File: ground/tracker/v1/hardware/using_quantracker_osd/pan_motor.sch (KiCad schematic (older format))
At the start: 20 parts, among them K4 CONN_3, P2 CONN_4, P3 CONN_5, U4 SI8620, U5 74AHC1G04

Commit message: add i2c and gps connectors
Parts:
- C18: renamed from C21; value C -> 0.1uF; footprint (none) -> SMD_0603:SMD_0603
- renumbered C22 to C19, C23 to C20, C24 to C21, C25 to C22, C26 to C23, C27 to C24, C28 to C25, C29 to C26
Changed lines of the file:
@@
 +5V
 $Comp
-L C C21
+L C C18
 U 1 1 587FB33F
 P 2325 7125
-F 0 "C21" H 2350 7225 50  0000 L CNN
-F 1 "C" H 2350 7025 50  0000 L CNN
-F 2 "" H 2363 6975 50  0000 C CNN
+F 0 "C18" H 2350 7225 50  0000 L CNN
+F 1 "0.1uF" H 2350 7025 50  0000 L CNN
+F 2 "SMD_0603:SMD_0603" H 2363 6975 50  0001 C CNN
 F 3 "" H 2325 7125 50  0000 C CNN
 	1    2325 7125
@@
 $EndComp
 $Comp
-L C C22
+L C C19
 U 1 1 587FB43C
 P 4525 3800
-F 0 "C22" H 4550 3900 50  0000 L CNN
+F 0 "C19" H 4550 3900 50  0000 L CNN
 F 1 "C" H 4550 3700 50  0000 L CNN
 F 2 "" H 4563 3650 50  0000 C CNN
@@
 $EndComp
 $Comp
-L C C23
+L C C20
 U 1 1 587FB7FF
 P 4800 3800
-F 0 "C23" H 4825 3900 50  0000 L CNN
+F 0 "C20" H 4825 3900 50  0000 L CNN
 F 1 "C" H 4825 3700 50  0000 L CNN
 F 2 "" H 4838 3650 50  0000 C CNN
@@
 $EndComp
 $Comp
-L CAP3T C25
+L CAP3T C22
 U 1 1 587FBE06
 P 6625 2125
-F 0 "C25" H 6775 1875 60  0000 C CNN
+F 0 "C22" H 6775 1875 60  0000 C CNN
 F 1 "NFM18PS105R0J3" H 6825 2375 60  0000 C CNN
 F 2 "" H 6625 2125 60  0001 C CNN
@@
 NoConn ~ 10125 5775
 $Comp
-L CAP3T C29
+L CAP3T C26
 U 1 1 587FE706
 P 9275 5075
-F 0 "C29" H 9425 4825 60  0000 C CNN
+F 0 "C26" H 9425 4825 60  0000 C CNN
 F 1 "NFM31PC276B0J3" H 9475 5325 60  0000 C CNN
 F 2 "" H 9275 5075 60  0001 C CNN
@@
 	6250 6225 5550 6225
 $Comp
-L CAP3T C24
+L CAP3T C21
 U 1 1 587FF1BF
 P 5300 6225
-F 0 "C24" H 5450 5975 60  0000 C CNN
+F 0 "C21" H 5450 5975 60  0000 C CNN
 F 1 "NFM18PS105R0J3" H 5500 6475 60  0000 C CNN
 F 2 "" H 5300 6225 60  0001 C CNN
@@
 	3750 5350 2075 5350
 $Comp
-L CP1 C27
+L CP1 C24
 U 1 1 58801015
 P 8450 5500
-F 0 "C27" H 8475 5600 50  0000 L CNN
+F 0 "C24" H 8475 5600 50  0000 L CNN
 F 1 "CP1" H 8475 5400 50  0000 L CNN
 F 2 "" H 8450 5500 50  0000 C CNN
@@
 $EndComp
 $Comp
-L CP1 C28
+L CP1 C25
 U 1 1 58801095
 P 8750 5500
-F 0 "C28" H 8775 5600 50  0000 L CNN
+F 0 "C25" H 8775 5600 50  0000 L CNN
 F 1 "CP1" H 8775 5400 50  0000 L CNN
 F 2 "" H 8750 5500 50  0000 C CNN
@@
 Pan Motor power
 $Comp
-L C C26
+L C C23
 U 1 1 5880246B
 P 7775 5525
-F 0 "C26" H 7800 5625 50  0000 L CNN
+F 0 "C23" H 7800 5625 50  0000 L CNN
 F 1 "C" H 7800 5425 50  0000 L CNN
 F 2 "" H 7813 5375 50  0000 C CNN
@@
 $EndComp
 $Comp
-L PWR_FLAG #FLG09
+L PWR_FLAG #FLG010
 U 1 1 58820405
 P 7825 4025
-F 0 "#FLG09" H 7825 4120 50  0001 C CNN
+F 0 "#FLG010" H 7825 4120 50  0001 C CNN
 F 1 "PWR_FLAG" H 7825 4205 50  0000 C CNN
 F 2 "" H 7825 4025 50  0000 C CNN
@@
 Connection ~ 7825 4225
 $Comp
-L PWR_FLAG #FLG010
+L PWR_FLAG #FLG011
 U 1 1 58820682
 P 8125 1950
-F 0 "#FLG010" H 8125 2045 50  0001 C CNN
+F 0 "#FLG011" H 8125 2045 50  0001 C CNN
 F 1 "PWR_FLAG" H 8125 2130 50  0000 C CNN
 F 2 "" H 8125 1950 50  0000 C CNN
@@
 Connection ~ 8125 2125
 $Comp
-L PWR_FLAG #FLG011
+L PWR_FLAG #FLG012
 U 1 1 58820928
 P 5025 2000
-F 0 "#FLG011" H 5025 2095 50  0001 C CNN
+F 0 "#FLG012" H 5025 2095 50  0001 C CNN
 F 1 "PWR_FLAG" H 5025 2180 50  0000 C CNN
 F 2 "" H 5025 2000 50  0000 C CNN

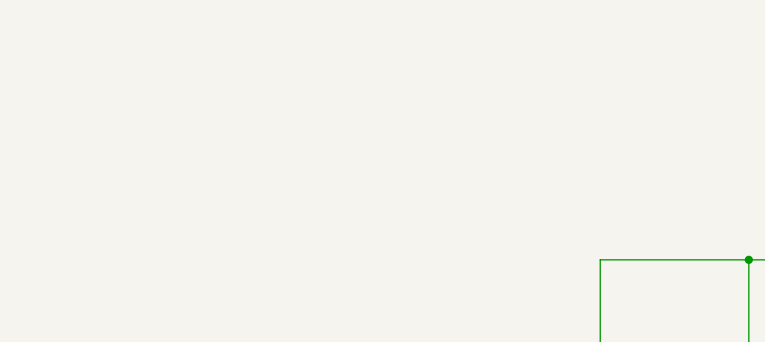
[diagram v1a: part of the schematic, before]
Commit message: add emf and currnt feedback opton
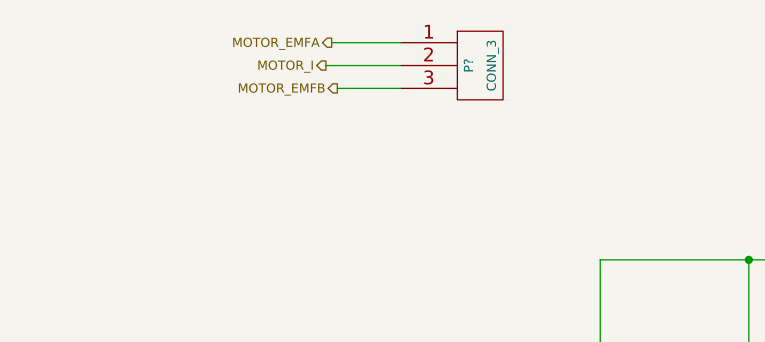
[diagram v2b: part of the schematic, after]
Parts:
- added P?: CONN_3, symbol CONN_3
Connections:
- new net MOTOR_EMFA: P?.1 (P1)
- new net MOTOR_EMFB: P?.3 (P3)
- new net MOTOR_I: P?.2 (PM)
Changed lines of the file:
@@
 	5025 2000 5025 2125
 Connection ~ 5025 2125
+$Comp
+L CONN_3 P?
+U 1 1 588A3767
+P 3350 1275
+F 0 "P?" V 3300 1275 40  0000 C CNN
+F 1 "CONN_3" V 3400 1275 40  0000 C CNN
+F 2 "" H 3350 1275 60  0001 C CNN
+F 3 "" H 3350 1275 60  0001 C CNN
+	1    3350 1275
+	1    0    0    -1
+$EndComp
+Text HLabel 2700 1175 0    40   Output ~ 0
+MOTOR_EMFA
+Text HLabel 2725 1375 0    40   Output ~ 0
+MOTOR_EMFB
+Wire Wire Line
+	3000 1175 2700 1175
+Wire Wire Line
+	3000 1375 2725 1375
+Text HLabel 2675 1275 0    40   Output ~ 0
+MOTOR_I
+Wire Wire Line
+	3000 1275 2675 1275
 $EndSCHEMATC

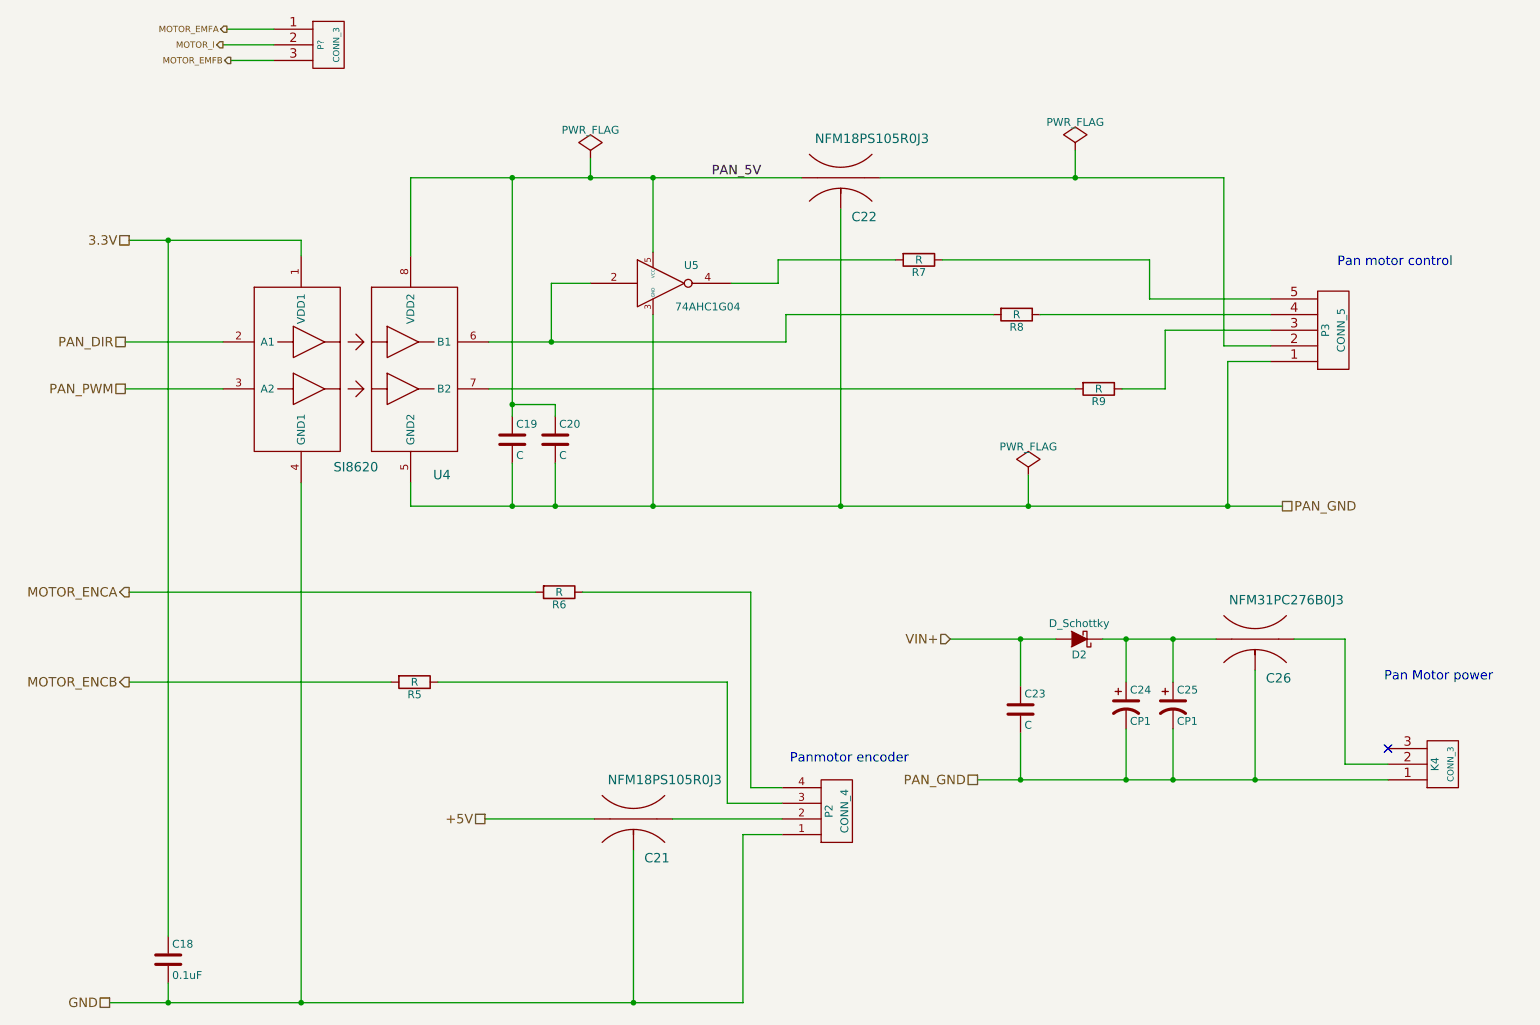
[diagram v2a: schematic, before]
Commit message: move encoder up out of pan motor schematic
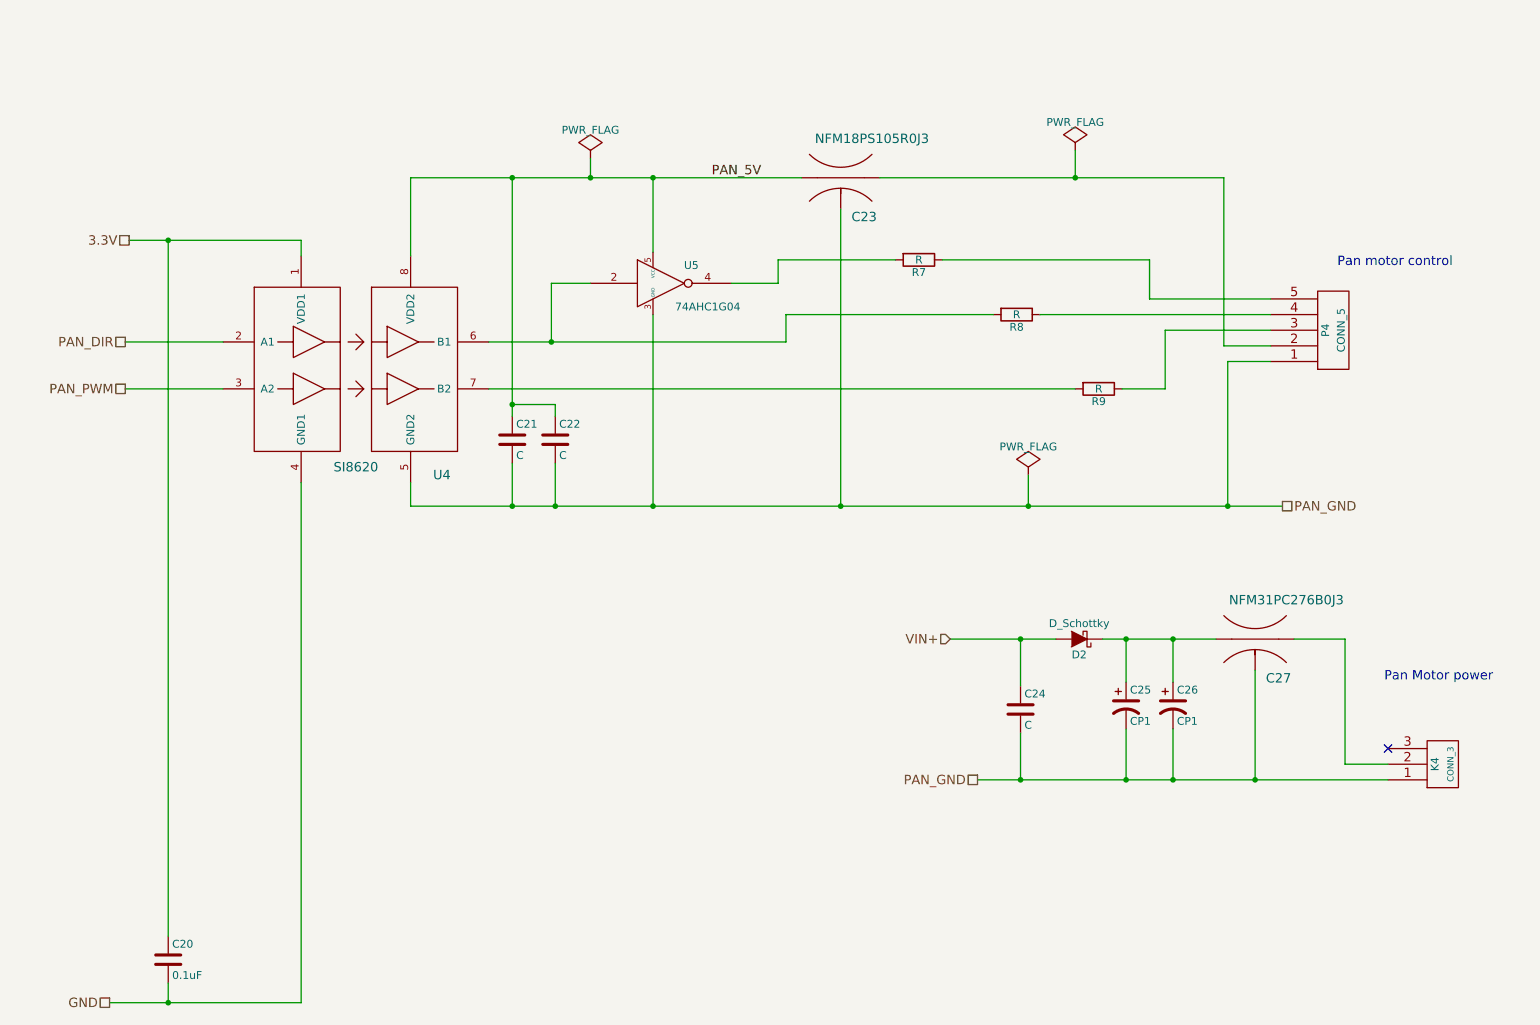
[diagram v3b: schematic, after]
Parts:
- removed C21: NFM18PS105R0J3, symbol CAP3T
- removed P2: CONN_4, symbol CONN_4
- removed P?: CONN_3, symbol CONN_3
- removed R5, R6: R, symbol R
- renumbered C18 to C20, C19 to C21, C20 to C22, C22 to C23, C23 to C24, C24 to C25, C25 to C26, C26 to C27, P3 to P4
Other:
- note removed: "Panmotor encoder"
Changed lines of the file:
@@
 $EndComp
 $Comp
-L CONN_5 P3
+L CONN_5 P4
 U 1 1 587F798A
 P 9775 3100
-F 0 "P3" V 9725 3100 50  0000 C CNN
+F 0 "P4" V 9725 3100 50  0000 C CNN
 F 1 "CONN_5" V 9825 3100 50  0000 C CNN
 F 2 "" H 9775 3100 60  0001 C CNN
@@
 	1    0    0    1
 $EndComp
-$Comp
-L CONN_4 P2
-U 1 1 587F7991
-P 6600 6175
-F 0 "P2" V 6550 6175 50  0000 C CNN
-F 1 "CONN_4" V 6650 6175 50  0000 C CNN
-F 2 "" H 6600 6175 60  0001 C CNN
-F 3 "" H 6600 6175 60  0001 C CNN
-	1    6600 6175
-	1    0    0    1
-$EndComp
 Text Notes 9800 2700 0    60   ~ 0
 Pan motor control
-Text Notes 6300 5875 0    60   ~ 0
-Panmotor encoder
 Text HLabel 2075 2525 0    60   UnSpc ~ 0
 3.3V
@@
 Text Label 5800 2125 0    60   ~ 0
 PAN_5V
-Text HLabel 2075 4775 0    60   Output ~ 0
-MOTOR_ENCA
-Text HLabel 2075 5350 0    60   Output ~ 0
-MOTOR_ENCB
-Text HLabel 4350 6225 0    60   UnSpc ~ 0
-+5V
-$Comp
-L C C18
+$Comp
+L C C20
 U 1 1 587FB33F
 P 2325 7125
-F 0 "C18" H 2350 7225 50  0000 L CNN
+F 0 "C20" H 2350 7225 50  0000 L CNN
 F 1 "0.1uF" H 2350 7025 50  0000 L CNN
 F 2 "SMD_0603:SMD_0603" H 2363 6975 50  0001 C CNN
@@
 $EndComp
 $Comp
-L C C19
+L C C21
 U 1 1 587FB43C
 P 4525 3800
-F 0 "C19" H 4550 3900 50  0000 L CNN
+F 0 "C21" H 4550 3900 50  0000 L CNN
 F 1 "C" H 4550 3700 50  0000 L CNN
 F 2 "" H 4563 3650 50  0000 C CNN
@@
 $EndComp
 $Comp
-L C C20
+L C C22
 U 1 1 587FB7FF
 P 4800 3800
-F 0 "C20" H 4825 3900 50  0000 L CNN
+F 0 "C22" H 4825 3900 50  0000 L CNN
 F 1 "C" H 4825 3700 50  0000 L CNN
 F 2 "" H 4838 3650 50  0000 C CNN
@@
 $EndComp
 $Comp
-L CAP3T C22
+L CAP3T C23
 U 1 1 587FBE06
 P 6625 2125
-F 0 "C22" H 6775 1875 60  0000 C CNN
+F 0 "C23" H 6775 1875 60  0000 C CNN
 F 1 "NFM18PS105R0J3" H 6825 2375 60  0000 C CNN
 F 2 "" H 6625 2125 60  0001 C CNN
@@
 	3875 4225 3875 4075
 Wire Wire Line
-	1950 7400 6000 7400
+	1950 7400 3175 7400
 Wire Wire Line
 	3175 7400 3175 4075
@@
 Wire Wire Line
 	6875 2125 9075 2125
-Connection ~ 3175 7400
 Wire Wire Line
 	2325 6975 2325 2525
@@
 NoConn ~ 10125 5775
 $Comp
-L CAP3T C26
+L CAP3T C27
 U 1 1 587FE706
 P 9275 5075
-F 0 "C26" H 9425 4825 60  0000 C CNN
+F 0 "C27" H 9425 4825 60  0000 C CNN
 F 1 "NFM31PC276B0J3" H 9475 5325 60  0000 C CNN
 F 2 "" H 9275 5075 60  0001 C CNN
@@
 	9275 5275 9275 5975
 Connection ~ 9275 5975
-Wire Wire Line
-	6250 6325 6000 6325
-Wire Wire Line
-	6000 6325 6000 7400
-Wire Wire Line
-	4350 6225 5050 6225
-Wire Wire Line
-	6250 6225 5550 6225
-$Comp
-L CAP3T C21
-U 1 1 587FF1BF
-P 5300 6225
-F 0 "C21" H 5450 5975 60  0000 C CNN
-F 1 "NFM18PS105R0J3" H 5500 6475 60  0000 C CNN
-F 2 "" H 5300 6225 60  0001 C CNN
-F 3 "" H 5300 6225 60  0001 C CNN
-	1    5300 6225
-	1    0    0    -1
-$EndComp
-Wire Wire Line
-	5300 6425 5300 7400
-Connection ~ 5300 7400
-Wire Wire Line
-	4675 4775 2075 4775
-Wire Wire Line
-	6250 6025 6050 6025
-Wire Wire Line
-	6050 6025 6050 4775
-Wire Wire Line
-	6050 4775 4975 4775
-Wire Wire Line
-	6250 6125 5900 6125
-Wire Wire Line
-	5900 6125 5900 5350
-Wire Wire Line
-	5900 5350 4050 5350
-Wire Wire Line
-	3750 5350 2075 5350
-$Comp
-L CP1 C24
+$Comp
+L CP1 C25
 U 1 1 58801015
 P 8450 5500
-F 0 "C24" H 8475 5600 50  0000 L CNN
+F 0 "C25" H 8475 5600 50  0000 L CNN
 F 1 "CP1" H 8475 5400 50  0000 L CNN
 F 2 "" H 8450 5500 50  0000 C CNN
@@
 $EndComp
 $Comp
-L CP1 C25
+L CP1 C26
 U 1 1 58801095
 P 8750 5500
-F 0 "C25" H 8775 5600 50  0000 L CNN
+F 0 "C26" H 8775 5600 50  0000 L CNN
 F 1 "CP1" H 8775 5400 50  0000 L CNN
 F 2 "" H 8750 5500 50  0000 C CNN
@@
 Pan Motor power
 $Comp
-L C C23
+L C C24
 U 1 1 5880246B
 P 7775 5525
-F 0 "C23" H 7800 5625 50  0000 L CNN
+F 0 "C24" H 7800 5625 50  0000 L CNN
 F 1 "C" H 7800 5425 50  0000 L CNN
 F 2 "" H 7813 5375 50  0000 C CNN
@@
 $EndComp
 $Comp
-L R R5
-U 1 1 5880E2B6
-P 3900 5350
-F 0 "R5" V 3980 5350 50  0000 C CNN
-F 1 "R" V 3900 5350 50  0000 C CNN
-F 2 "" V 3830 5350 50  0000 C CNN
-F 3 "" H 3900 5350 50  0000 C CNN
-	1    3900 5350
-	0    1    1    0
-$EndComp
-$Comp
-L R R6
-U 1 1 5880E333
-P 4825 4775
-F 0 "R6" V 4905 4775 50  0000 C CNN
-F 1 "R" V 4825 4775 50  0000 C CNN
-F 2 "" V 4755 4775 50  0000 C CNN
-F 3 "" H 4825 4775 50  0000 C CNN
-	1    4825 4775
-	0    1    1    0
-$EndComp
-$Comp
-L PWR_FLAG #FLG010
+L PWR_FLAG #FLG012
 U 1 1 58820405
 P 7825 4025
-F 0 "#FLG010" H 7825 4120 50  0001 C CNN
+F 0 "#FLG012" H 7825 4120 50  0001 C CNN
 F 1 "PWR_FLAG" H 7825 4205 50  0000 C CNN
 F 2 "" H 7825 4025 50  0000 C CNN
@@
 Connection ~ 7825 4225
 $Comp
-L PWR_FLAG #FLG011
+L PWR_FLAG #FLG013
 U 1 1 58820682
 P 8125 1950
-F 0 "#FLG011" H 8125 2045 50  0001 C CNN
+F 0 "#FLG013" H 8125 2045 50  0001 C CNN
 F 1 "PWR_FLAG" H 8125 2130 50  0000 C CNN
 F 2 "" H 8125 1950 50  0000 C CNN
@@
 Connection ~ 8125 2125
 $Comp
-L PWR_FLAG #FLG012
+L PWR_FLAG #FLG014
 U 1 1 58820928
 P 5025 2000
-F 0 "#FLG012" H 5025 2095 50  0001 C CNN
+F 0 "#FLG014" H 5025 2095 50  0001 C CNN
 F 1 "PWR_FLAG" H 5025 2180 50  0000 C CNN
 F 2 "" H 5025 2000 50  0000 C CNN
@@
 	5025 2000 5025 2125
 Connection ~ 5025 2125
-$Comp
-L CONN_3 P?
-U 1 1 588A3767
-P 3350 1275
-F 0 "P?" V 3300 1275 40  0000 C CNN
-F 1 "CONN_3" V 3400 1275 40  0000 C CNN
-F 2 "" H 3350 1275 60  0001 C CNN
-F 3 "" H 3350 1275 60  0001 C CNN
-	1    3350 1275
-	1    0    0    -1
-$EndComp
-Text HLabel 2700 1175 0    40   Output ~ 0
-MOTOR_EMFA
-Text HLabel 2725 1375 0    40   Output ~ 0
-MOTOR_EMFB
-Wire Wire Line
-	3000 1175 2700 1175
-Wire Wire Line
-	3000 1375 2725 1375
-Text HLabel 2675 1275 0    40   Output ~ 0
-MOTOR_I
-Wire Wire Line
-	3000 1275 2675 1275
 $EndSCHEMATC
